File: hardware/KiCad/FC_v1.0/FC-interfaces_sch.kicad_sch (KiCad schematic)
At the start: 39 parts, among them J10 PAD_OUT, J11 PAD_OUT, J12 PAD_OUT_Mini, J13 PAD_OUT_Mini, J2 MEM2061-01-188-00-A, J3 USB4105-GF-A, J4 Conn_ARM_SWD_TagConnect_TC203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, J5 SM06B-GHS-TB, J6 SM04B-GHS-TB, J7 SM06B-GHS-TB, J8 SM06B-GHS-TB, J9 SM04B-GHS-TB, Q1 AO3400A, U8 USBLC6-2SC6

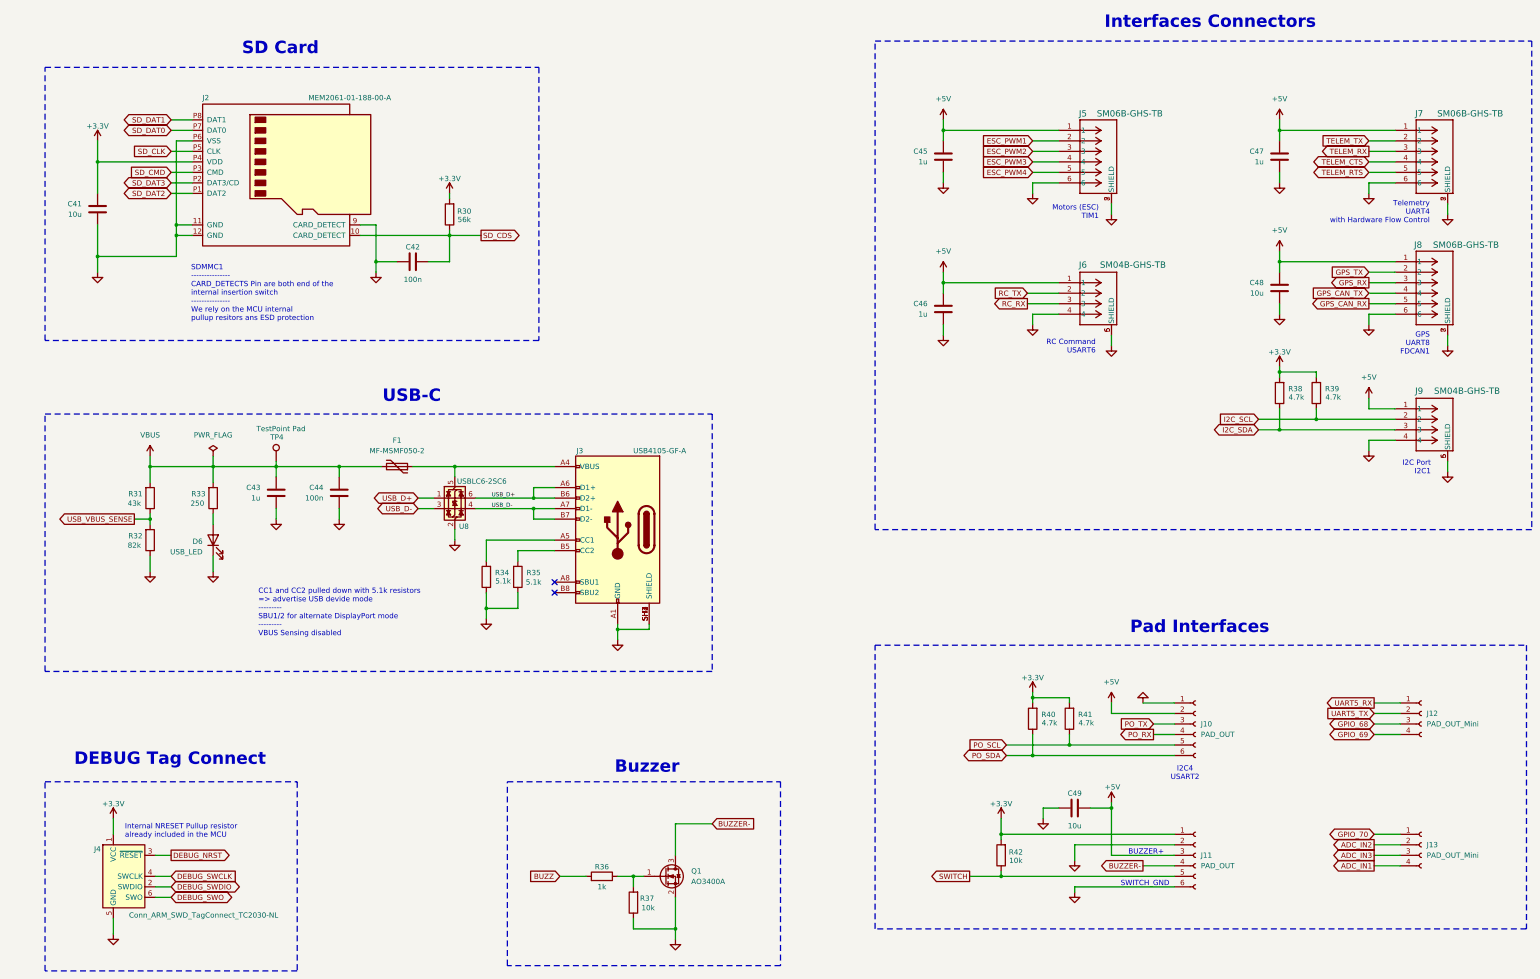
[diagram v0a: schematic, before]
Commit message: changing USB ESD IC (v0.8)
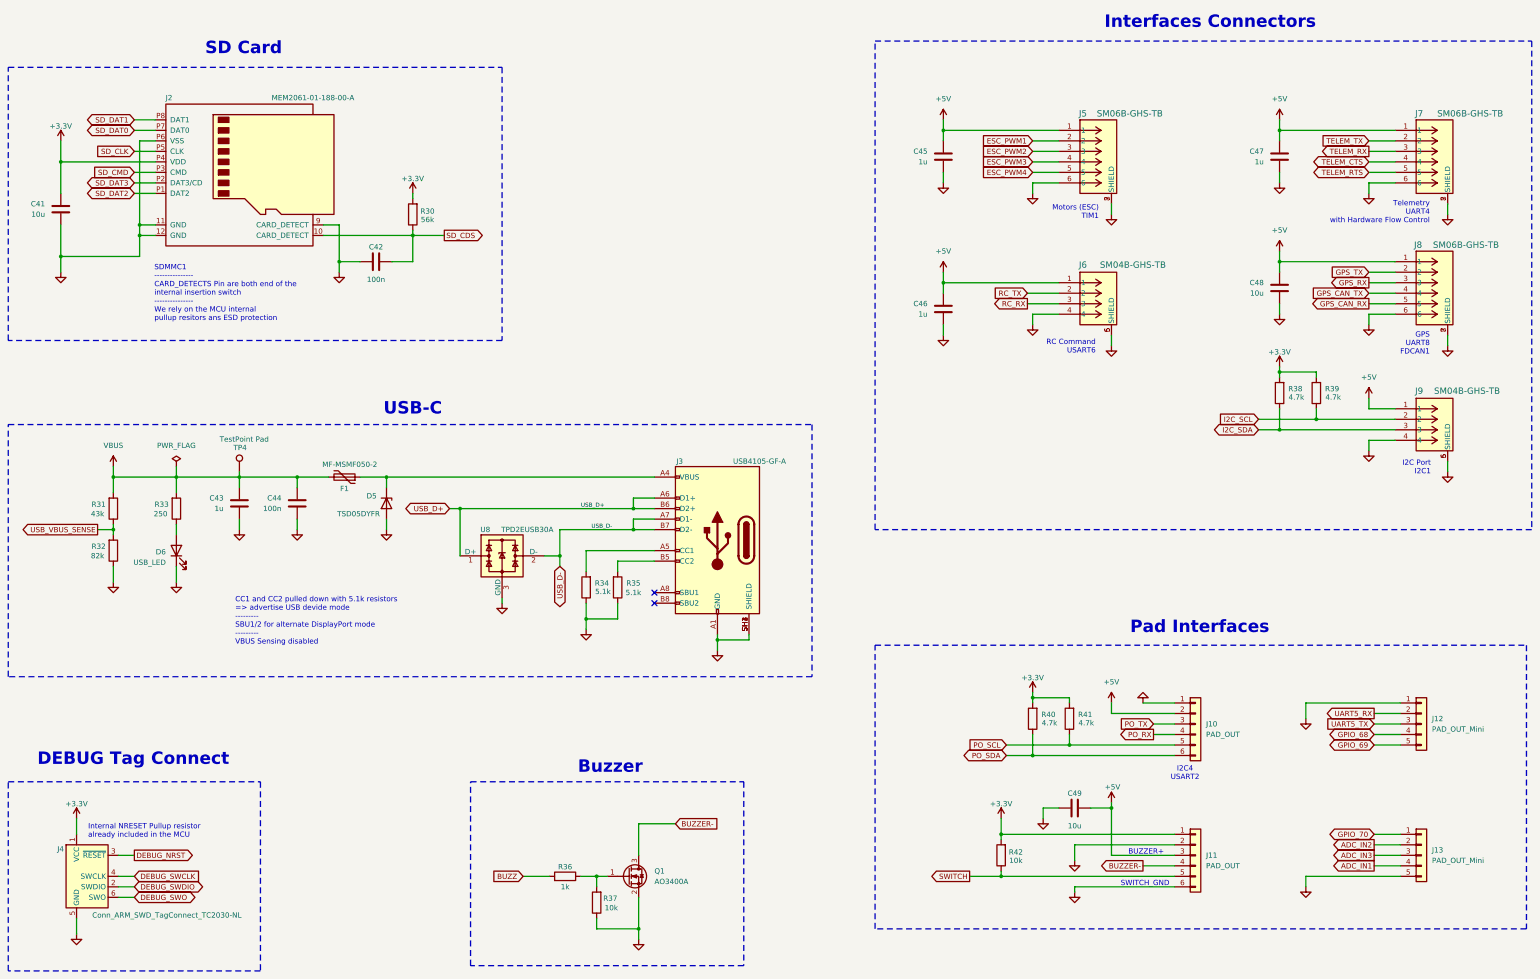
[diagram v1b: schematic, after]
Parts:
- removed J10, J11: PAD_OUT, FC-FootprintLib:Pad_out_1x6, symbol Connector:Conn_01x06_Socket
- removed J12, J13: PAD_OUT_Mini, FC-FootprintLib:Pad_out_mini_1x4, symbol Connector:Conn_01x04_Socket
- removed U8: USBLC6-2SC6, Package_TO_SOT_SMD:SOT-23-6, symbol FC-SchemSymbolLib:USBLC6-2SC6
- added D5: TSD05DYFR, FC-FootprintLib:TVS_SOD2_DYF_TEX, symbol Diode:ESD5Zxx
- added J10, J11: PAD_OUT, FC-FootprintLib:Pad_out_1x6, symbol Connector_Generic:Conn_01x06
- added J12, J13: PAD_OUT_Mini, FC-FootprintLib:Pad_out_mini_1x5, symbol Connector_Generic:Conn_01x05
- added U8: TPD2EUSB30A, Package_TO_SOT_SMD:Texas_DRT-3, symbol Power_Protection:TPD2EUSB30A
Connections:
- net +3.3V: now also J11.1 (Pin_1)
- net +5V: now also J10.2 (Pin_2), J11.3 (Pin_3)
- net ADC_IN1: now also J13.4 (Pin_4)
- net ADC_IN2: now also J13.2 (Pin_2)
- net ADC_IN3: now also J13.3 (Pin_3)
- net BUZZER-: now also J11.4 (Pin_4)
- net GND: now also D5.2 (A), J10.1 (Pin_1), J11.2 (Pin_2), J11.6 (Pin_6), J12.1 (Pin_1), J13.5 (Pin_5), U8.3 (GND)
- net GPIO_68: now also J12.4 (Pin_4)
- net GPIO_69: now also J12.5 (Pin_5)
- net GPIO_70: now also J13.1 (Pin_1)
- net PO_RX: now also J10.4 (Pin_4)
- net PO_SCL: now also J10.5 (Pin_5)
- net PO_SDA: now also J10.6 (Pin_6)
- net PO_TX: now also J10.3 (Pin_3)
- net SWITCH: now also J11.5 (Pin_5)
- net UART5_RX: now also J12.2 (Pin_2)
- net UART5_TX: now also J12.3 (Pin_3)
- net USB_D+: now also U8.1 (D+)
- net USB_D-: now also U8.2 (D-)
- net at F1.1, J3.A4 (VBUS), J3.B4 (VBUS): now also D5.1 (K)
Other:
- moved on the sheet: C41, C42, C43, C44, D6, F1, J2, J3, J4, Q1, R30, R31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

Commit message: Component library update
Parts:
- removed C41, C48, C49: 10u, Capacitor_SMD:C_0603_1608Metric, symbol Device:C
- removed C42, C44: 100n, Capacitor_SMD:C_0402_1005Metric, symbol Device:C
- removed C43, C45, C46, C47: 1u, Capacitor_SMD:C_0402_1005Metric, symbol Device:C
- removed R30: 56k, Resistor_SMD:R_0402_1005Metric, symbol Device:R
- removed R31: 43k, Resistor_SMD:R_0402_1005Metric, symbol Device:R
- removed R32: 82k, Resistor_SMD:R_0402_1005Metric, symbol Device:R
- removed R33: 250, Resistor_SMD:R_0402_1005Metric, symbol Device:R
- removed R34, R35: 5.1k, Resistor_SMD:R_0402_1005Metric, symbol Device:R
- removed R36: 1k, Resistor_SMD:R_0402_1005Metric, symbol Device:R
- removed R37, R42: 10k, Resistor_SMD:R_0402_1005Metric, symbol Device:R
- removed R38, R39, R40, R41: 4.7k, Resistor_SMD:R_0402_1005Metric, symbol Device:R
- added C41, C48, C49: 10u, Capacitor_SMD:C_0603_1608Metric, symbol FC-SchemSymbolLib:CL10A106MA8NRNC
- added C42, C44: 100n, Capacitor_SMD:C_0402_1005Metric, symbol FC-SchemSymbolLib:CL05B104KO5NNNC
- added C43, C45, C46, C47: 1u, Capacitor_SMD:C_0402_1005Metric, symbol FC-SchemSymbolLib:CL05A105KA5NQNC
- added R30: 51k, Resistor_SMD:R_0402_1005Metric, symbol FC-SchemSymbolLib:0402WGF5102TCE
- added R31, R34, R35: 5.1k, Resistor_SMD:R_0402_1005Metric, symbol FC-SchemSymbolLib:0402WGF5101TCE
- added R32, R37, R42: 10k, Resistor_SMD:R_0402_1005Metric, symbol FC-SchemSymbolLib:0402WGF1002TCE
- added R33: 220, Resistor_SMD:R_0402_1005Metric, symbol FC-SchemSymbolLib:0402WGF2200TCE
- added R36: 1k, Resistor_SMD:R_0402_1005Metric, symbol FC-SchemSymbolLib:0402WGF1001TCE
- added R38, R39, R40, R41: 4.7k, Resistor_SMD:R_0402_1005Metric, symbol FC-SchemSymbolLib:0402WGF4701TCE
- D5: value TSD05DYFR -> ESD5Zxx; footprint FC-FootprintLib:TVS_SOD2_DYF_TEX -> Diode_SMD:D_SOD-523
- D6: value USB_LED -> LED
- F1: value MF-MSMF050-2 -> Polyfuse
- J10, J11: value PAD_OUT -> Conn_01x06
- J12, J13: value PAD_OUT_Mini -> Conn_01x05
- TP4: value TestPoint Pad -> TestPoint
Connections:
- net +3.3V: now also C41.2, R30.1, R38.1, R39.1, R40.1, R41.1, R42.1
- net +5V: now also C45.1, C46.1, C47.1, C48.2, C49.1
- net BUZZ: now also R36.1
- net GND: now also C41.1, C42.1, C43.2, C44.2, C45.2, C46.2, C47.2, C48.1, C49.2, R32.2, R34.2, R35.2, R37.2
- net I2C_SCL: now also R39.2
- net I2C_SDA: now also R38.2
- net PO_SCL: now also R41.2
- net PO_SDA: now also R40.2
- net SD_CDS: now also C42.2, R30.2
- net SWITCH: now also R42.2
- net USB_VBUS_SENSE: now also R31.2, R32.1
- net VBUS: now also C43.1, C44.1, R31.1, R33.1
- net at D6.2 (A): now also R33.2
- net at Q1.1 (G): now also R36.2, R37.1
- net at J3.B5 (CC2): now also R35.1
- net at J3.A5 (CC1): now also R34.1
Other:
- moved on the sheet: D6, TP4

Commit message: Schematic update v0.9
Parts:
- removed D5: ESD5Zxx, Diode_SMD:D_SOD-523, symbol Diode:ESD5Zxx
- removed D6: LED, LED_SMD:LED_0603_1608Metric, symbol Device:LED
- removed F1: Polyfuse, Resistor_SMD:R_1812_4532Metric, symbol Device:Polyfuse
- removed Q1: AO3400A, Package_TO_SOT_SMD:SOT-23, symbol Transistor_FET:AO3400A
- removed U8: TPD2EUSB30A, Package_TO_SOT_SMD:Texas_DRT-3, symbol Power_Protection:TPD2EUSB30A
- added D5: LTVS16H5, FC-FootprintLib:DFN1610-2, symbol FC-SchemSymbolLib:LTVS16H5
- added D6: KT-0603R, LED_SMD:LED_0603_1608Metric, symbol FC-SchemSymbolLib:KT-0603R
- added F1: MF-MSMF050-2, symbol FC-SchemSymbolLib:MF-MSMF050-2
- added Q1: AO3400A, Package_TO_SOT_SMD:SOT-23-3, symbol FC-SchemSymbolLib:AO3400A
- added U8: TPD2EUSB30, Package_TO_SOT_SMD:Texas_DRT-3, symbol FC-SchemSymbolLib:TPD2EUSB30
- J10, J11, J12, J13: now left out of the parts list
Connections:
- net BUZZER-: now also Q1.3 (D)
- net GND: now also D5.2 (A), D6.1 (K), Q1.2 (S), U8.3 (GND)
- net USB_D+: now also U8.1 (D+)
- net USB_D-: now also U8.2 (D-)
- net VBUS: now also F1.1
- net at R36.2, R37.1: now also Q1.1 (G)
- net at R33.2: now also D6.2 (A)
- net at J3.A4 (VBUS), J3.B4 (VBUS): now also D5.1 (K), F1.2

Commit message: manufacturing exports v0.9
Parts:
- F1: footprint (none) -> Fuse:Fuse_1812_4532Metric
- J10, J11, J12, J13, J4: now not fitted
- J2, J3, J5, J6, J7, J8, J9, TP4: now not fitted; now left out of the parts list
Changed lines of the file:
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@@
 		(unit 1)
 		(exclude_from_sim no)
-		(in_bom yes)
+		(in_bom no)
 		(on_board yes)
-		(dnp no)
+		(dnp yes)
 		(property "Reference" "J2"
 			(at 68.072 45.466 0)
@@
 		(in_bom no)
 		(on_board yes)
-		(dnp no)
+		(dnp yes)
 		(fields_autoplaced yes)
 		(property "Reference" "J10"
@@
 		(in_bom no)
 		(on_board yes)
-		(dnp no)
+		(dnp yes)
 		(fields_autoplaced yes)
 		(property "Reference" "J11"
@@
 		(unit 1)
 		(exclude_from_sim no)
-		(in_bom yes)
+		(in_bom no)
 		(on_board yes)
-		(dnp no)
+		(dnp yes)
 		(property "Reference" "J9"
 			(at 369.316 116.332 0)
@@
 		(unit 1)
 		(exclude_from_sim no)
-		(in_bom yes)
+		(in_bom no)
 		(on_board yes)
-		(dnp no)
+		(dnp yes)
 		(property "Reference" "J7"
 			(at 369.316 49.276 0)
@@
 		(unit 1)
 		(exclude_from_sim no)
-		(in_bom yes)
+		(in_bom no)
 		(on_board yes)
-		(dnp no)
+		(dnp yes)
 		(property "Reference" "J5"
 			(at 288.036 49.276 0)
@@
 			)
 		)
-		(property "Footprint" ""
+		(property "Footprint" "Fuse:Fuse_1812_4532Metric"
 			(at 119.38 130.302 0)
 			(show_name yes)
@@
 		(in_bom no)
 		(on_board yes)
-		(dnp no)
+		(dnp yes)
 		(fields_autoplaced yes)
 		(property "Reference" "J13"
@@
 		(unit 1)
 		(exclude_from_sim no)
-		(in_bom yes)
+		(in_bom no)
 		(on_board yes)
-		(dnp no)
+		(dnp yes)
 		(property "Reference" "J8"
 			(at 369.062 81.026 0)
@@
 		(unit 1)
 		(exclude_from_sim no)
-		(in_bom yes)
+		(in_bom no)
 		(on_board yes)
-		(dnp no)
+		(dnp yes)
 		(property "Reference" "J3"
 			(at 191.516 133.35 0)
@@
 		(in_bom no)
 		(on_board yes)
-		(dnp no)
+		(dnp yes)
 		(property "Reference" "J4"
 			(at 42.672 227.076 0)
@@
 		(unit 1)
 		(exclude_from_sim no)
-		(in_bom yes)
+		(in_bom no)
 		(on_board yes)
-		(dnp no)
+		(dnp yes)
 		(property "Reference" "TP4"
 			(at 89.408 130.048 0)
@@
 		(unit 1)
 		(exclude_from_sim no)
-		(in_bom yes)
+		(in_bom no)
 		(on_board yes)
-		(dnp no)
+		(dnp yes)
 		(property "Reference" "J6"
 			(at 288.036 85.852 0)
@@
 		(in_bom no)
 		(on_board yes)
-		(dnp no)
+		(dnp yes)
 		(fields_autoplaced yes)
 		(property "Reference" "J12"
